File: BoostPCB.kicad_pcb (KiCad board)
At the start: 2 copper layers, 51 x 25 mm, 3 parts, among them J1 Conn_01x03_Pin, J2 Conn_01x03_Pin, U1 BoostConverter

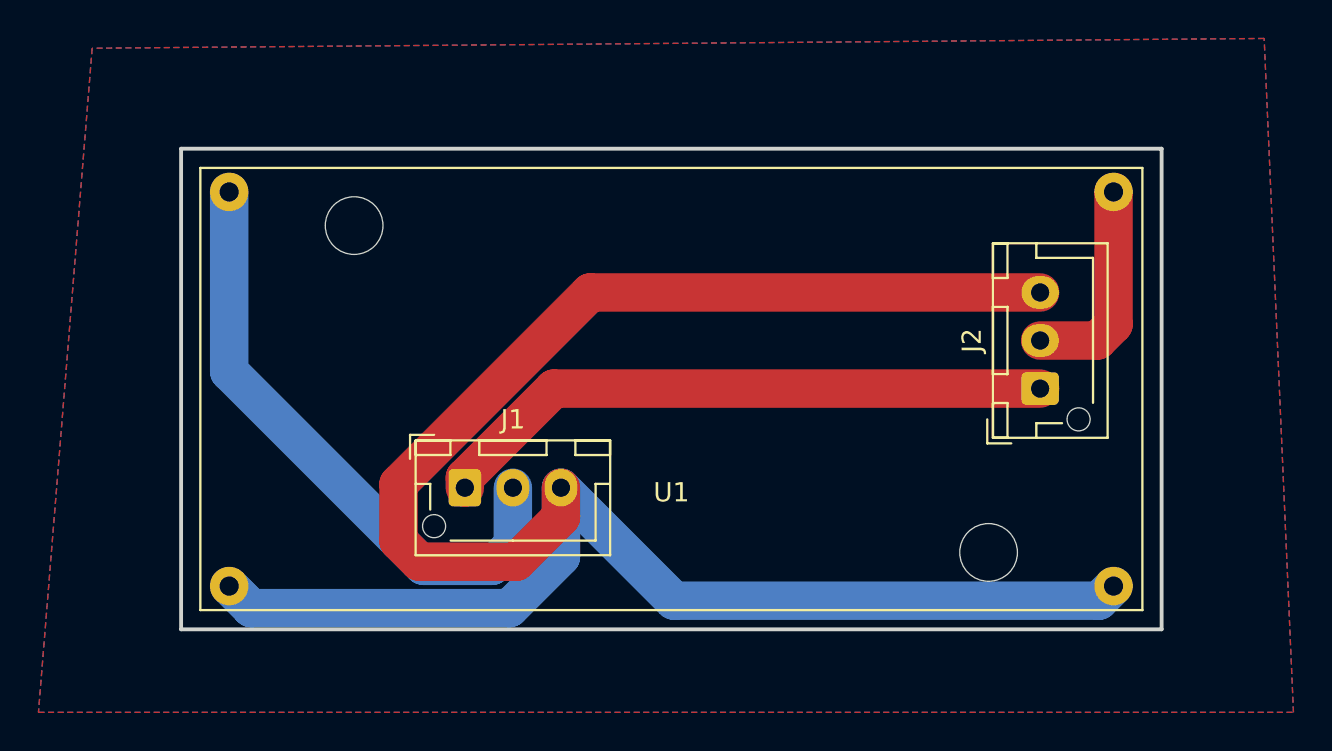
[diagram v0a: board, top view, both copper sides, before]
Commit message: Fixed connector side
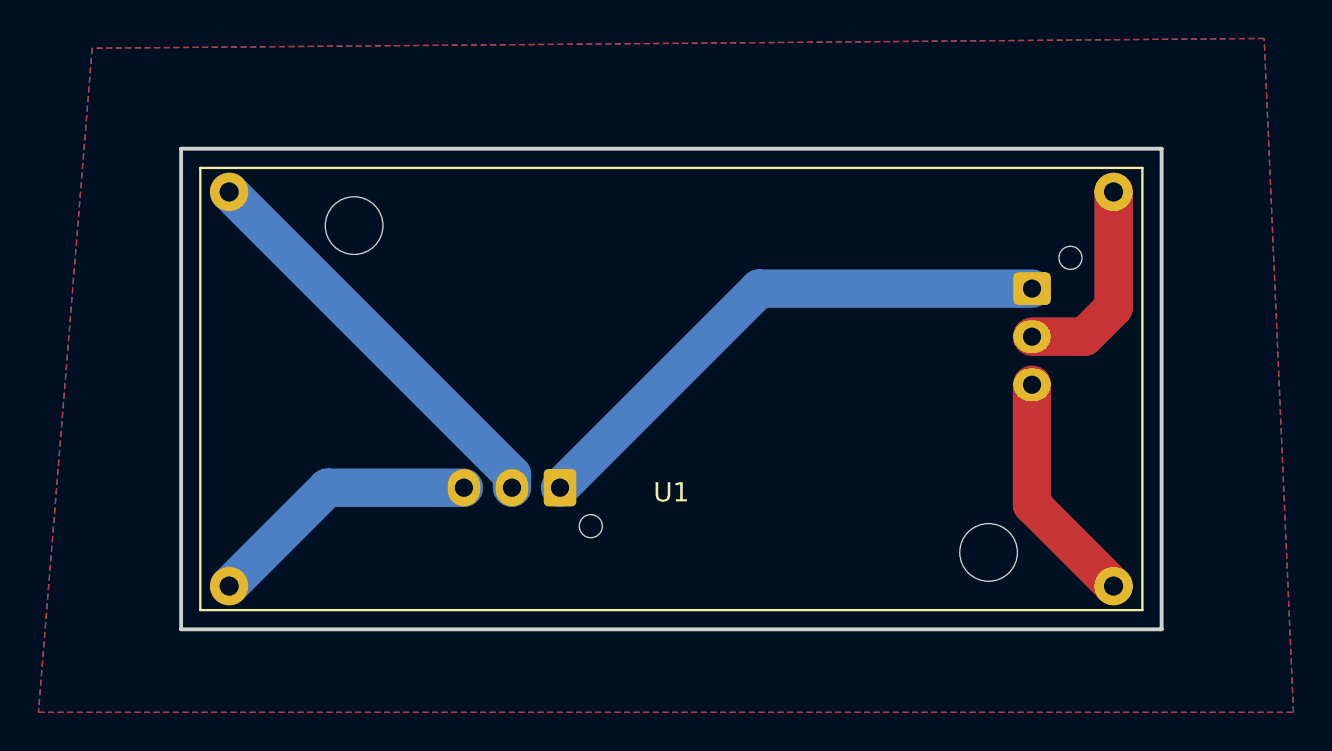
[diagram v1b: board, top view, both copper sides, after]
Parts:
- J1, J2: moved to B.Cu
- moved J2 5.22 mm to (154.6, 82.1), turned to -90 degrees
- moved J1 4.95 mm to (130.0, 92.5), turned to 180 degrees
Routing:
- net GND: track 105.8 -> 26.6 mm
- net 12v: track 31.7 -> 21.5 mm
- net Kicker: track 32.4 -> 28.8 mm
